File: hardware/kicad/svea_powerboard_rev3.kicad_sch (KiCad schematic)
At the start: 0 parts

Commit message: nearly done cleaning
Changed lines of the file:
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@@
 	)
 	(sheet
-		(at 10 15)
+		(at 8.73 18.81)
 		(size 82 18)
 		(exclude_from_sim no)
@@
 		)
 		(property "Sheetname" "Battery System"
-			(at 10 14.2884 0)
+			(at 8.73 18.0984 0)
 			(effects
 				(font
@@
 		)
 		(property "Sheetfile" "sheets/modules/01_Battery-System.kicad_sch"
-			(at 10 33.5846 0)
+			(at 8.73 37.3946 0)
 			(effects
 				(font
@@
 	)
 	(sheet
-		(at 10 67)
-		(size 82 18)
+		(at 32.86 61.92)
+		(size 56.04 33.33)
 		(exclude_from_sim no)
 		(in_bom yes)
@@
 		)
 		(property "Sheetname" "MCU Control"
-			(at 10 66.2884 0)
+			(at 32.86 61.2084 0)
 			(effects
 				(font
@@
 		)
 		(property "Sheetfile" "sheets/modules/04_MCU-Control.kicad_sch"
-			(at 10 85.5846 0)
+			(at 32.86 95.8346 0)
 			(effects
 				(font
@@
 	)
 	(sheet
-		(at 102 67)
-		(size 82 18)
+		(at 136.29 59.38)
+		(size 84.69 47.3)
 		(exclude_from_sim no)
 		(in_bom yes)
@@
 		)
 		(property "Sheetname" "External IO"
-			(at 102 66.2884 0)
+			(at 136.29 58.6684 0)
 			(effects
 				(font
@@
 		)
 		(property "Sheetfile" "sheets/modules/05_External-IO.kicad_sch"
-			(at 102 85.5846 0)
+			(at 136.29 107.2646 0)
 			(effects
 				(font

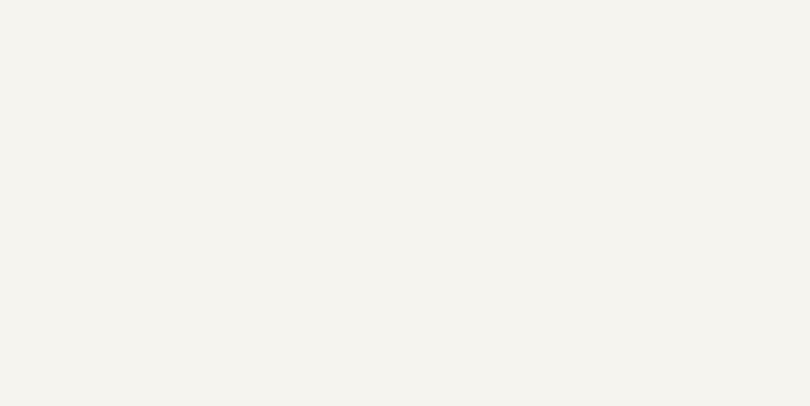
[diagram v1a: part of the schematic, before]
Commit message: better sheet nesting for power rails
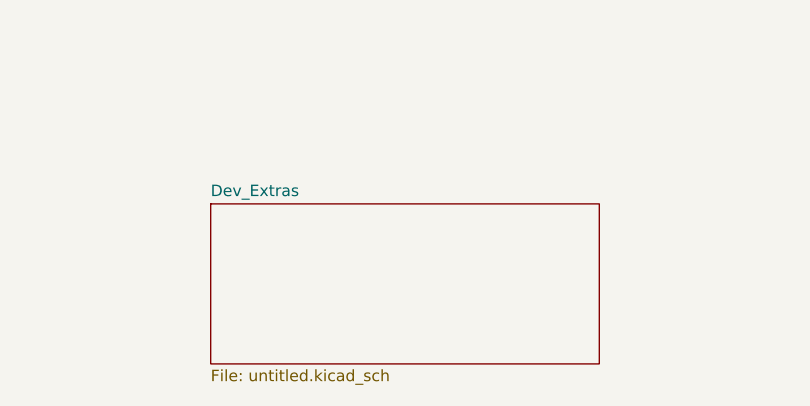
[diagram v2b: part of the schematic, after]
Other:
- added sheet Dev_Extras (untitled.kicad_sch)
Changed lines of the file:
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@@
+	)
+	(sheet
+		(at 50.8 125.73)
+		(size 43.18 17.78)
+		(exclude_from_sim yes)
+		(in_bom no)
+		(on_board yes)
+		(dnp no)
+		(fields_autoplaced yes)
+		(stroke
+			(width 0.1524)
+			(type solid)
+		)
+		(fill
+			(color 0 0 0 0.0000)
+		)
+		(property "Sheetname" "Dev_Extras"
+			(at 50.8 125.0184 0)
+			(effects
+				(font
+					(size 1.27 1.27)
+				)
+				(justify left bottom)
+			)
+		)
+		(property "Sheetfile" "untitled.kicad_sch"
+			(at 50.8 144.0946 0)
+			(effects
+				(font
+					(size 1.27 1.27)
+				)
+				(justify left top)
+			)
+		)
+		(instances
+			(project "svea_powerboard_rev3"
+				(path "/3f85abf4-0b95-4c4a-b7e9-06f59ca1ea3d"
+					(page "29")
+				)
+			)
+		)
 	)
 	(sheet

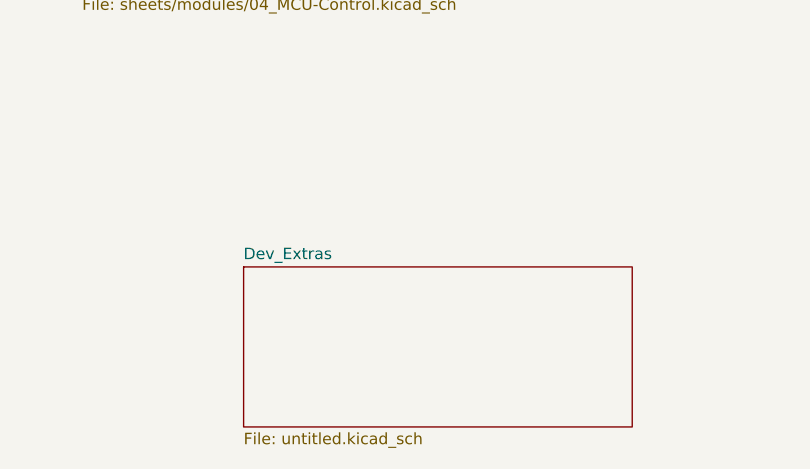
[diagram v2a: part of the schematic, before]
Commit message: netties and better sheet nesting for servo connectors
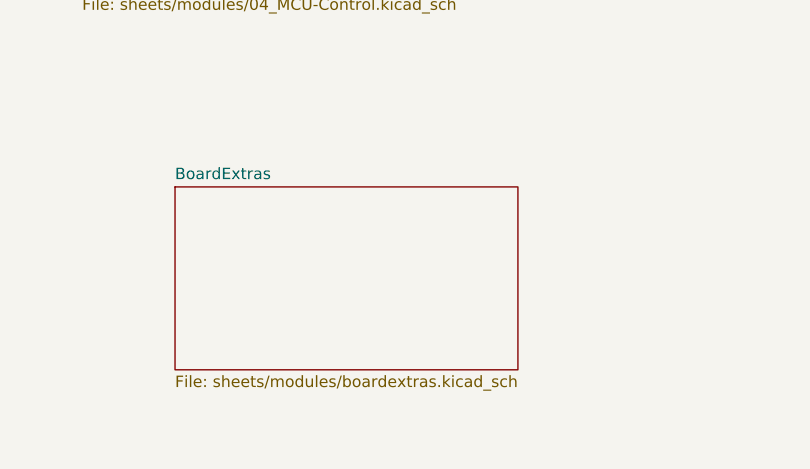
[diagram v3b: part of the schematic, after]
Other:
- removed sheet Dev_Extras
- added sheet BoardExtras (sheets/modules/boardextras.kicad_sch)
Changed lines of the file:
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@@
-	)
-	(sheet
-		(at 50.8 125.73)
-		(size 43.18 17.78)
-		(exclude_from_sim yes)
-		(in_bom no)
-		(on_board yes)
-		(dnp no)
-		(fields_autoplaced yes)
-		(stroke
-			(width 0.1524)
-			(type solid)
-		)
-		(fill
-			(color 0 0 0 0.0000)
-		)
-		(property "Sheetname" "Dev_Extras"
-			(at 50.8 125.0184 0)
-			(effects
-				(font
-					(size 1.27 1.27)
-				)
-				(justify left bottom)
-			)
-		)
-		(property "Sheetfile" "untitled.kicad_sch"
-			(at 50.8 144.0946 0)
-			(effects
-				(font
-					(size 1.27 1.27)
-				)
-				(justify left top)
-			)
-		)
-		(instances
-			(project "svea_powerboard_rev3"
-				(path "/3f85abf4-0b95-4c4a-b7e9-06f59ca1ea3d"
-					(page "29")
-				)
-			)
-		)
 	)
 	(sheet
@@
 				)
 			)
+		)
+	)
+	(sheet
+		(at 43.18 116.84)
+		(size 38.1 20.32)
+		(exclude_from_sim no)
+		(in_bom yes)
+		(on_board yes)
+		(dnp no)
+		(fields_autoplaced yes)
+		(stroke
+			(width 0.1524)
+			(type solid)
+		)
+		(fill
+			(color 0 0 0 0.0000)
+		)
+		(property "Sheetname" "BoardExtras"
+			(at 43.18 116.1284 0)
+			(effects
+				(font
+					(size 1.27 1.27)
+				)
+				(justify left bottom)
+			)
+		)
+		(property "Sheetfile" "sheets/modules/boardextras.kicad_sch"
+			(at 43.18 137.7446 0)
+			(effects
+				(font
+					(size 1.27 1.27)
+				)
+				(justify left top)
+			)
+		)
+		(instances
+			(project "svea_powerboard_rev3"
+				(path "/3f85abf4-0b95-4c4a-b7e9-06f59ca1ea3d"
+					(page "31")
+				)
+			)

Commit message: various improvements
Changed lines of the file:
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@@
 	)
 	(sheet
-		(at 8.73 18.81)
+		(at 13.81 26.43)
 		(size 82 18)
 		(exclude_from_sim no)
@@
 		)
 		(property "Sheetname" "Battery System"
-			(at 8.73 18.0984 0)
+			(at 13.81 25.7184 0)
 			(effects
 				(font
@@
 		)
 		(property "Sheetfile" "sheets/modules/01_Battery-System.kicad_sch"
-			(at 8.73 37.3946 0)
+			(at 13.81 45.0146 0)
 			(effects
 				(font

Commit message: starting pcb
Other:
- removed sheet BoardExtras
- removed sheet Charging Input
- removed sheet External IO
- removed sheet MCU Control
- removed sheet Power Rails
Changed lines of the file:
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@@
-		)
-	)
-	(sheet
-		(at 102 15)
-		(size 82 18)
-		(exclude_from_sim no)
-		(in_bom yes)
-		(on_board yes)
-		(dnp no)
-		(fields_autoplaced yes)
-		(stroke
-			(width 0)
-			(type solid)
-		)
-		(fill
-			(color 0 0 0 0.0000)
-		)
-		(property "Sheetname" "Power Rails"
-			(at 102 14.2884 0)
-			(effects
-				(font
-					(size 1.27 1.27)
-				)
-				(justify left bottom)
-			)
-		)
-		(property "Sheetfile" "sheets/modules/02_Power-Rails.kicad_sch"
-			(at 102 33.5846 0)
-			(effects
-				(font
-					(size 1.27 1.27)
-				)
-				(justify left top)
-			)
-		)
-		(instances
-			(project "svea_powerboard_rev3"
-				(path "/3f85abf4-0b95-4c4a-b7e9-06f59ca1ea3d"
-					(page "2")
-				)
-			)
-		)
-	)
-	(sheet
-		(at 194 15)
-		(size 82 18)
-		(exclude_from_sim no)
-		(in_bom yes)
-		(on_board yes)
-		(dnp no)
-		(fields_autoplaced yes)
-		(stroke
-			(width 0)
-			(type solid)
-		)
-		(fill
-			(color 0 0 0 0.0000)
-		)
-		(property "Sheetname" "Charging Input"
-			(at 194 14.2884 0)
-			(effects
-				(font
-					(size 1.27 1.27)
-				)
-				(justify left bottom)
-			)
-		)
-		(property "Sheetfile" "sheets/modules/03_Charging-Input.kicad_sch"
-			(at 194 33.5846 0)
-			(effects
-				(font
-					(size 1.27 1.27)
-				)
-				(justify left top)
-			)
-		)
-		(instances
-			(project "svea_powerboard_rev3"
-				(path "/3f85abf4-0b95-4c4a-b7e9-06f59ca1ea3d"
-					(page "3")
-				)
-			)
-		)
-	)
-	(sheet
-		(at 32.86 61.92)
-		(size 56.04 33.33)
-		(exclude_from_sim no)
-		(in_bom yes)
-		(on_board yes)
-		(dnp no)
-		(fields_autoplaced yes)
-		(stroke
-			(width 0)
-			(type solid)
-		)
-		(fill
-			(color 0 0 0 0.0000)
-		)
-		(property "Sheetname" "MCU Control"
-			(at 32.86 61.2084 0)
-			(effects
-				(font
-					(size 1.27 1.27)
-				)
-				(justify left bottom)
-			)
-		)
-		(property "Sheetfile" "sheets/modules/04_MCU-Control.kicad_sch"
-			(at 32.86 95.8346 0)
-			(effects
-				(font
-					(size 1.27 1.27)
-				)
-				(justify left top)
-			)
-		)
-		(instances
-			(project "svea_powerboard_rev3"
-				(path "/3f85abf4-0b95-4c4a-b7e9-06f59ca1ea3d"
-					(page "4")
-				)
-			)
-		)
-	)
-	(sheet
-		(at 136.29 59.38)
-		(size 84.69 47.3)
-		(exclude_from_sim no)
-		(in_bom yes)
-		(on_board yes)
-		(dnp no)
-		(fields_autoplaced yes)
-		(stroke
-			(width 0)
-			(type solid)
-		)
-		(fill
-			(color 0 0 0 0.0000)
-		)
-		(property "Sheetname" "External IO"
-			(at 136.29 58.6684 0)
-			(effects
-				(font
-					(size 1.27 1.27)
-				)
-				(justify left bottom)
-			)
-		)
-		(property "Sheetfile" "sheets/modules/05_External-IO.kicad_sch"
-			(at 136.29 107.2646 0)
-			(effects
-				(font
-					(size 1.27 1.27)
-				)
-				(justify left top)
-			)
-		)
-		(instances
-			(project "svea_powerboard_rev3"
-				(path "/3f85abf4-0b95-4c4a-b7e9-06f59ca1ea3d"
-					(page "5")
-				)
-			)
-		)
-	)
-	(sheet
-		(at 43.18 116.84)
-		(size 38.1 20.32)
-		(exclude_from_sim no)
-		(in_bom yes)
-		(on_board yes)
-		(dnp no)
-		(fields_autoplaced yes)
-		(stroke
-			(width 0.1524)
-			(type solid)
-		)
-		(fill
-			(color 0 0 0 0.0000)
-		)
-		(property "Sheetname" "BoardExtras"
-			(at 43.18 116.1284 0)
-			(effects
-				(font
-					(size 1.27 1.27)
-				)
-				(justify left bottom)
-			)
-		)
-		(property "Sheetfile" "sheets/modules/boardextras.kicad_sch"
-			(at 43.18 137.7446 0)
-			(effects
-				(font
-					(size 1.27 1.27)
-				)
-				(justify left top)
-			)
-		)
-		(instances
-			(project "svea_powerboard_rev3"
-				(path "/3f85abf4-0b95-4c4a-b7e9-06f59ca1ea3d"
-					(page "31")
-				)
-			)
 		)
 	)
